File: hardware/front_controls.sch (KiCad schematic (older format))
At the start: 87 parts, among them J1 Conn_01x02, J2 Conn_01x02, J3 Conn_01x02, J4 Conn_01x02, J5 Conn_01x02, J6 Conn_01x02, J7 Conn_01x02, J8 Conn_01x02, J9 Conn_01x02, P2 CONN_01X10, Q1 Q_PNP_BEC, U1 Adafruit_Metro_Mini, U10 G3VM-31BR, U2 G3VM-31BR, U3 G3VM-31BR, U4 G3VM-31BR, U5 G3VM-31BR, U6 G3VM-31BR, U7 G3VM-31BR, U8 G3VM-31BR, U9 G3VM-31BR

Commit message: Version 2 hardware files
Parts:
- removed D20, D21: D_Schottky, Diode_SMD:D_SMC, symbol Device:D_Schottky
- removed Q1: Q_PNP_BEC, Package_TO_SOT_SMD:SOT-23, symbol Device:Q_PNP_BEC
- removed U1: Adafruit_Metro_Mini, Adafruit:DIP-28_W15.24mm, symbol front_controls-rescue:Adafruit_Metro_Mini
- added A1: Arduino_Nano_v3.x, NANO:Arduino_Nano, symbol MCU_Module:Arduino_Nano_v3.x
- added C11, C12: 33pf, Capacitor_SMD:C_0402_1005Metric, symbol Device:C_Small
- added C13, C14, C15, C16: 100nf, Capacitor_SMD:C_0402_1005Metric, symbol Device:C_Small
- added C17: 330uf, Capacitor_THT:CP_Radial_D8.0mm_P3.50mm, symbol Device:CP1_Small
- added Cboot1: 0.1uf, Capacitor_SMD:C_0402_1005Metric, symbol Device:C
- added Chf1: 220nf, Capacitor_SMD:C_0805_2012Metric, symbol Device:C
- added Cin1: 10uf, Capacitor_SMD:C_0805_2012Metric, symbol Device:C
- added Cout1, Cout2, Cout3, Cout4: 22uF, Capacitor_SMD:C_0805_2012Metric, symbol Device:C
- added D20: 15V standoff, Diode_SMD:D_SMB, symbol Device:D_TVS
- added J10: Conn_01x02, Connector_PinHeader_2.54mm:PinHeader_1x02_P2.54mm_Vertical, symbol Connector_Generic:Conn_01x02
- added L1: 8uH, 14m, Inductor_SMD:L_Bourns_SRP7028A_7.3x6.6mm, symbol Device:L_Small
- added P1: PWR, Connector_JST:JST_EH_B2B-EH-A_1x02_P2.50mm_Vertical, symbol Connector_Generic:Conn_01x02
- added P3: HM-10, Connector_PinSocket_2.54mm:PinSocket_1x06_P2.54mm_Vertical, symbol Connector_Generic:Conn_01x06
- added P4: Conn_01x06, Connector_PinHeader_2.54mm:PinHeader_1x06_P2.54mm_Vertical, symbol Connector_Generic:Conn_01x06
- added R10, R14, R15, R18, R19, R9: 1k, Resistor_SMD:R_0402_1005Metric, symbol Device:R
- added R42: 4K7 1%, Resistor_SMD:R_0402_1005Metric, symbol front_controls-rescue:R
- added R43, R44: 100k, Resistor_SMD:R_0402_1005Metric, symbol front_controls-rescue:R
- added Rfbb1: 24K9 1%, Resistor_SMD:R_0402_1005Metric, symbol Device:R
- added Rfbt1: 100k 1%, Resistor_SMD:R_0402_1005Metric, symbol Device:R
- added U12: LMR33630ADDA, NANO:Texas_HSOP-8-1EP_3.9x4.9mm_P1.27mm_ThermalVias, symbol Regulators:LMR33630ADDA
- added U13: MCP23017-E/SO, Package_SO:SOIC-28W_7.5x18.7mm_P1.27mm, symbol Interface_Expansion:MCP23017_SO
- added U14: MCP2515-xSO, Package_SO:SOIC-18W_7.5x11.6mm_P1.27mm, symbol Interface_CAN_LIN:MCP2515-xSO
- added U15: TJA1051T, Package_SO:SOIC-8_3.9x4.9mm_P1.27mm, symbol Interface_CAN_LIN:TJA1051T
- added Y1: 12Mhz, Crystal:Crystal_SMD_3225-4Pin_3.2x2.5mm, symbol Device:Crystal_GND24_Small
- D1, D14, D15, D16, D17, D18, D19, D2, D3, D4, D5, D6: footprint Diode_SMD:D_SMC -> Diode_SMD:D_SOD-123; LCSC C35722 -> C8598
- D10, D11, D12, D13, D8, D9: value 4.7 -> 4.7V Zener; footprint Diode_SMD:D_SMB -> Diode_SMD:D_SOD-323; LCSC C188530 -> C136181
- D7: value 5.1 -> 5.1V Zener
- R0: renamed from R1; value 500 -> 500R
- R1: renamed from R2; value 500 -> 500R
- R2: renamed from R3; value 500 -> 500R
- R24: value 10 -> 10R
- R27: renamed from R25; value 10 -> 10R
- R3: renamed from R30; value 500 -> 500R
- R30: renamed from R26; value 10 -> 10R
- R33: renamed from R27; value 10 -> 10R
- R36: renamed from R28; value 10 -> 10R
- R39: renamed from R29; value 10 -> 10R
- R4: renamed from R31; value 500 -> 500R
- R40: renamed from R10; value 10 -> 10R
- R5: renamed from R32; value 500 -> 500R
- R6: renamed from R33; value 500 -> 500R
- R7: renamed from R34; value 500 -> 500R
- R8: renamed from R35; value 500 -> 500R
- renumbered R4 to R12, R7 to R13, R5 to R16, R8 to R17, R6 to R20, R9 to R21, R12 to R22, R18 to R23, R13 to R25, R19 to R26, R14 to R28, R20 to R29, R15 to R31, R21 to R32, R16 to R34, R22 to R35, R17 to R37, R23 to R38, R11 to R41
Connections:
- net GND: now also A1.29 (GND), A1.4 (GND), C11.1, C12.1, C13.2, C14.1, C15.2, C16.2, C17.2, Chf1.1, Cin1.1, Cout1.2, Cout2.2, Cout3.2, Cout4.2, D20.1 (A1), P1.1 (Pin_1), P3.4 (Pin_4), P4.6 (Pin_6), R10.2, R15.2, R19.2, R42.2, Rfbb1.2, U12.1 (PGND), U12.9 (AGND), U13.10 (VSS), U14.9 (VSS), U15.2 (GND), U15.8 (S), Y1.2, Y1.4; no longer D2.2 (A), D4.2 (A), D6.2 (A)
- net VCC: now also A1.27 (+5V), C13.1, C14.2, C15.1, C16.1, Cout1.1, Cout2.1, Cout3.1, Cout4.1, L1.1, P3.5 (Pin_5), R43.2, R44.1, Rfbt1.2, U13.9 (VDD), U14.18 (VDD), U15.3 (VCC)
- net OUT_U7: now reaches U7.1
- net OUT_U7: now also U13.6 (GPB5)
- net OUT_U8: now reaches U8.1
- net OUT_U8: now also U13.7 (GPB6)
- net OUT_U9: now reaches U9.1
- net OUT_U9: now also U13.8 (GPB7)
- net OUT_U10: now reaches U10.1
- net OUT_U10: now also U13.21 (GPA0)
- net IN_AN1: now reaches C4.1, D7.1 (K), R40.2, R41.1
- net IN_AN1: now also A1.25 (A6)
- net IN_LOW1: now reaches C1.1, R12.2, R13.2
- net IN_LOW1: now also U13.22 (GPA1)
- net IN_LOW2: now reaches C2.1, R16.2, R17.2
- net IN_LOW2: now also U13.23 (GPA2)
- net IN_LOW3: now reaches C3.1, R20.2, R21.2
- net IN_LOW3: now also U13.24 (GPA3)
- net OUT_U3: now reaches U3.1
- net OUT_U3: now also U13.2 (GPB1)
- net OUT_U4: now reaches U4.1
- net OUT_U4: now also U13.3 (GPB2)
- net IN_HIGH6: now reaches C10.1, D13.1 (K), R37.1, R38.1
- net IN_HIGH6: now also A1.5 (D2)
- net IN_HIGH5: now reaches C9.1, D12.1 (K), R34.1, R35.1
- net IN_HIGH5: now also A1.7 (D4)
- net IN_HIGH4: now reaches C8.1, D11.1 (K), R31.1, R32.1
- net IN_HIGH4: now also A1.8 (D5)
- net IN_HIGH3: now reaches C7.1, D10.1 (K), R28.1, R29.1
- net IN_HIGH3: now also U13.27 (GPA6)
- net IN_HIGH2: now reaches C6.1, D9.1 (K), R25.1, R26.1
- net IN_HIGH2: now also U13.26 (GPA5)
- net IN_HIGH1: now reaches C5.1, D8.1 (K), R22.1, R23.1
- net IN_HIGH1: now also U13.25 (GPA4)
- net OUT_U5: now reaches U5.1
- net OUT_U5: now also U13.4 (GPB3)
- net OUT_U6: now reaches U6.1
- net OUT_U6: now also U13.5 (GPB4)
- net at P2.10 (P10): now also R9.2; no longer D1.1 (K)
- net at P2.8 (P8): now also R18.2; no longer D5.1 (K)
- net at P2.9 (P9): now also R14.2; no longer D3.1 (K)
- net OUT_U2: now reaches U2.1
- net OUT_U2: now also U13.1 (GPB0)
- new net: D1.1 (K), R9.1
- new net: D2.2 (A), R10.1
- new net: D3.1 (K), R14.1
- new net: D4.2 (A), R15.1
- new net: D5.1 (K), R18.1
- new net: D6.2 (A), R19.1
- new net: C17.1, Chf1.2, Cin1.2, D20.2 (A2), P1.2 (Pin_2), U12.2 (VIN), U12.3 (EN)
- new net: Rfbb1.1, Rfbt1.1, U12.5 (FB)
- new net: Cboot1.1, L1.2, U12.7 (BOOT)
- new net: Cboot1.2, U12.8 (SW)
- new net: R42.1, U13.15 (A0), U13.16 (A1), U13.17 (A2)
- new net: R44.2, U13.18 (~RESET~)
- new net: R43.1, U14.17 (~RESET)
- new net: C12.2, U14.7 (OSC2), Y1.3
- new net: C11.2, U14.8 (OSC1), Y1.1
- new net BT_EN: A1.12 (D9), P3.6 (Pin_6)
- new net BT_RX: A1.10 (D7), P3.2 (Pin_2)
- new net BT_STATE: P3.1 (Pin_1), U13.28 (GPA7)
- new net BT_TX: A1.11 (D8), P3.3 (Pin_3)
- new net CAN_H: J10.1 (Pin_1), U15.7 (CANH)
- new net CAN_INT: A1.20 (A1), U14.12 (~INT)
- new net CAN_L: J10.2 (Pin_2), U15.6 (CANL)
- new net INTA1: A1.6 (D3), U13.20 (INTA)
- new net OUT_11: A1.9 (D6), P4.1 (Pin_1)
- new net OUT_12: A1.26 (A7), P4.2 (Pin_2)
- new net OUT_13: A1.22 (A3), P4.3 (Pin_3)
- new net OUT_14: A1.21 (A2), P4.4 (Pin_4)
- new net OUT_15: A1.19 (A0), P4.5 (Pin_5)
- new net RXCAN: U14.2 (RXCAN), U15.4 (RXD)
- new net SCL: A1.24 (A5), U13.12 (SCK)
- new net SDA: A1.23 (A4), U13.13 (SDA)
- new net SPI_CS: A1.13 (D10), U14.16 (~CS)
- new net SPI_SCK: A1.16 (D13), U14.13 (SCK)
- new net SPI_SI: A1.14 (D11), U14.14 (SI)
- new net SPI_SO: A1.15 (D12), U14.15 (SO)
- new net TXCAN: U14.1 (TXCAN), U15.1 (TXD)
- no-connect marks 8 -> 0
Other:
- moved on the sheet: C4, D7, R40, R41

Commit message: Hardware V2 major modifications
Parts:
- removed C17: 330uf, Capacitor_THT:CP_Radial_D8.0mm_P3.50mm, symbol Device:CP1_Small
- removed Cboot1: 0.1uf, Capacitor_SMD:C_0402_1005Metric, symbol Device:C
- removed Chf1: 220nf, Capacitor_SMD:C_0805_2012Metric, symbol Device:C
- removed Cin1: 10uf, Capacitor_SMD:C_0805_2012Metric, symbol Device:C
- removed Cout1, Cout2, Cout3, Cout4: 22uF, Capacitor_SMD:C_0805_2012Metric, symbol Device:C
- removed D20: 15V standoff, Diode_SMD:D_SMB, symbol Device:D_TVS
- removed L1: 8uH, 14m, Inductor_SMD:L_Bourns_SRP7028A_7.3x6.6mm, symbol Device:L_Small
- removed Rfbb1: 24K9 1%, Resistor_SMD:R_0402_1005Metric, symbol Device:R
- removed Rfbt1: 100k 1%, Resistor_SMD:R_0402_1005Metric, symbol Device:R
- removed U12: LMR33630ADDA, NANO:Texas_HSOP-8-1EP_3.9x4.9mm_P1.27mm_ThermalVias, symbol Regulators:LMR33630ADDA
- added H? (x4): MountingHole, MountingHole:MountingHole_2.7mm_M2.5, symbol Mechanical:MountingHole
- added J11: CAN, Connector_JST:JST_EH_B2B-EH-A_1x02_P2.50mm_Vertical, symbol Connector_Generic:Conn_01x02
- added JP1: Jumper_NO_Small, Jumper:SolderJumper-2_P1.3mm_Open_RoundedPad1.0x1.5mm, symbol Device:Jumper_NO_Small
- added P2: PWR, Connector_JST:JST_EH_B2B-EH-A_1x02_P2.50mm_Vertical, symbol Connector_Generic:Conn_01x02
- added R11, R45: 4k7, Resistor_SMD:R_0603_1608Metric, symbol Device:R_Small
- added R46: 120R, Resistor_SMD:R_0402_1005Metric, symbol Device:R_Small
- added U1: TXB0104PW, Package_SO:TSSOP-14_4.4x5mm_P0.65mm, symbol Logic_LevelTranslator:TXB0104PW
- C4: value .01uf -> .1uf; LCSC C15195 -> C1525
- H3: renamed from P4; value Conn_01x06 -> Expansion; footprint Connector_PinHeader_2.54mm:PinHeader_1x06_P2.54mm_Vertical -> Connector_PinHeader_2.54mm:PinHeader_2x08_P2.54mm_Vertical; symbol Connector_Generic:Conn_01x06 -> Connector_Generic:Conn_02x08_Odd_Even
- J10: value Conn_01x02 -> CAN; footprint Connector_PinHeader_2.54mm:PinHeader_1x02_P2.54mm_Vertical -> Connector_JST:JST_EH_B2B-EH-A_1x02_P2.50mm_Vertical
- R40: value 10R -> 10k; footprint Resistor_SMD:R_0402_1005Metric -> Resistor_SMD:R_0603_1608Metric; LCSC C25077 -> C25804
- R41: value 1k -> 2k2; footprint Resistor_SMD:R_0402_1005Metric -> Resistor_SMD:R_0603_1608Metric; LCSC C11702 -> C4190
- renumbered P2 to H1, P3 to H2
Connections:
- net CAN_H: now also J11.1 (Pin_1), JP1.1
- net CAN_L: now also J11.2 (Pin_2), R46.1
- net GND: now also H3.1 (Pin_1), H3.14 (Pin_14), P2.1 (Pin_1), U1.7 (GND); no longer H3.6 (Pin_6), P1.1 (Pin_1)
- net SCL: now also H3.7 (Pin_7), R11.1
- net SDA: now also H3.9 (Pin_9), R45.2
- net SPI_SCK: now also H3.12 (Pin_12)
- net SPI_SI: now also H3.8 (Pin_8)
- net SPI_SO: now also H3.10 (Pin_10)
- net VCC: now also H3.2 (Pin_2), R11.2, R45.1, U1.14 (VCCB), U1.8 (OE)
- net VIN: now reaches P1.2 (Pin_2)
- net VIN: now also H3.16 (Pin_16), P2.2 (Pin_2)
- net UART_TX: now reaches A1.1 (D1/TX)
- net UART_TX: now also H3.6 (Pin_6)
- net 3V3: now reaches A1.17 (3V3)
- net 3V3: now also U1.1 (VCCA)
- net UART_RX: now reaches A1.2 (D0/RX)
- net UART_RX: now also H3.4 (Pin_4)
- net BT_RX renamed BT_RX_H
- net BT_RX_H: now also U1.12 (B2); no longer H2.2 (Pin_2)
- net BT_TX renamed BT_TX_H
- net BT_TX_H: now also U1.13 (B1); no longer H2.3 (Pin_3)
- net IN_HIGH1 renamed IN_HORN
- net IN_HIGH2 renamed IN_HL_HIGH
- net IN_HIGH3 renamed IN_KILL
- net IN_HIGH4 renamed IN_RIGHT
- net IN_HIGH5 renamed IN_LEFT
- net IN_HIGH6 renamed IN_BRAKE
- net IN_LOW1 renamed IN_CLUTCH
- net IN_LOW2 renamed IN_KICK
- net IN_LOW3 renamed IN_NEUTRAL
- net OUT_11 renamed MCU_D6
- net MCU_D6: now also H3.3 (Pin_3); no longer H3.1 (Pin_1)
- net OUT_12 renamed MCU_A7
- net MCU_A7: now also H3.5 (Pin_5); no longer H3.2 (Pin_2)
- net OUT_13 renamed MCU_A3
- net MCU_A3: now also H3.11 (Pin_11); no longer H3.3 (Pin_3)
- net OUT_14 renamed MCU_A2
- net MCU_A2: now also H3.13 (Pin_13); no longer H3.4 (Pin_4)
- net OUT_15 renamed MCU_A0
- net MCU_A0: now also H3.15 (Pin_15); no longer H3.5 (Pin_5)
- net OUT_U10 renamed OUT_HORN
- net OUT_U2 renamed OUT_LEFT
- net OUT_U3 renamed OUT_RIGHT
- net OUT_U4 renamed OUT_REAR
- net OUT_U5 renamed OUT_BRAKE
- net OUT_U6 renamed OUT_START_EN
- net OUT_U7 renamed OUT_HL_HIGH
- net OUT_U8 renamed OUT_HL_LOW
- net OUT_U9 renamed OUT_RUNNING
- new net: JP1.2, R46.2
- new net BT_RX_L: H2.2 (Pin_2), U1.3 (A2)
- new net BT_TX_L: H2.3 (Pin_3), U1.2 (A1)
- new net Switching Regulator (5V)/GND: P1.1 (Pin_1)
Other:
- moved on the sheet: A1, C11, C12, C13, C14, C15, C16, H2, R42, R43, R44, U13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

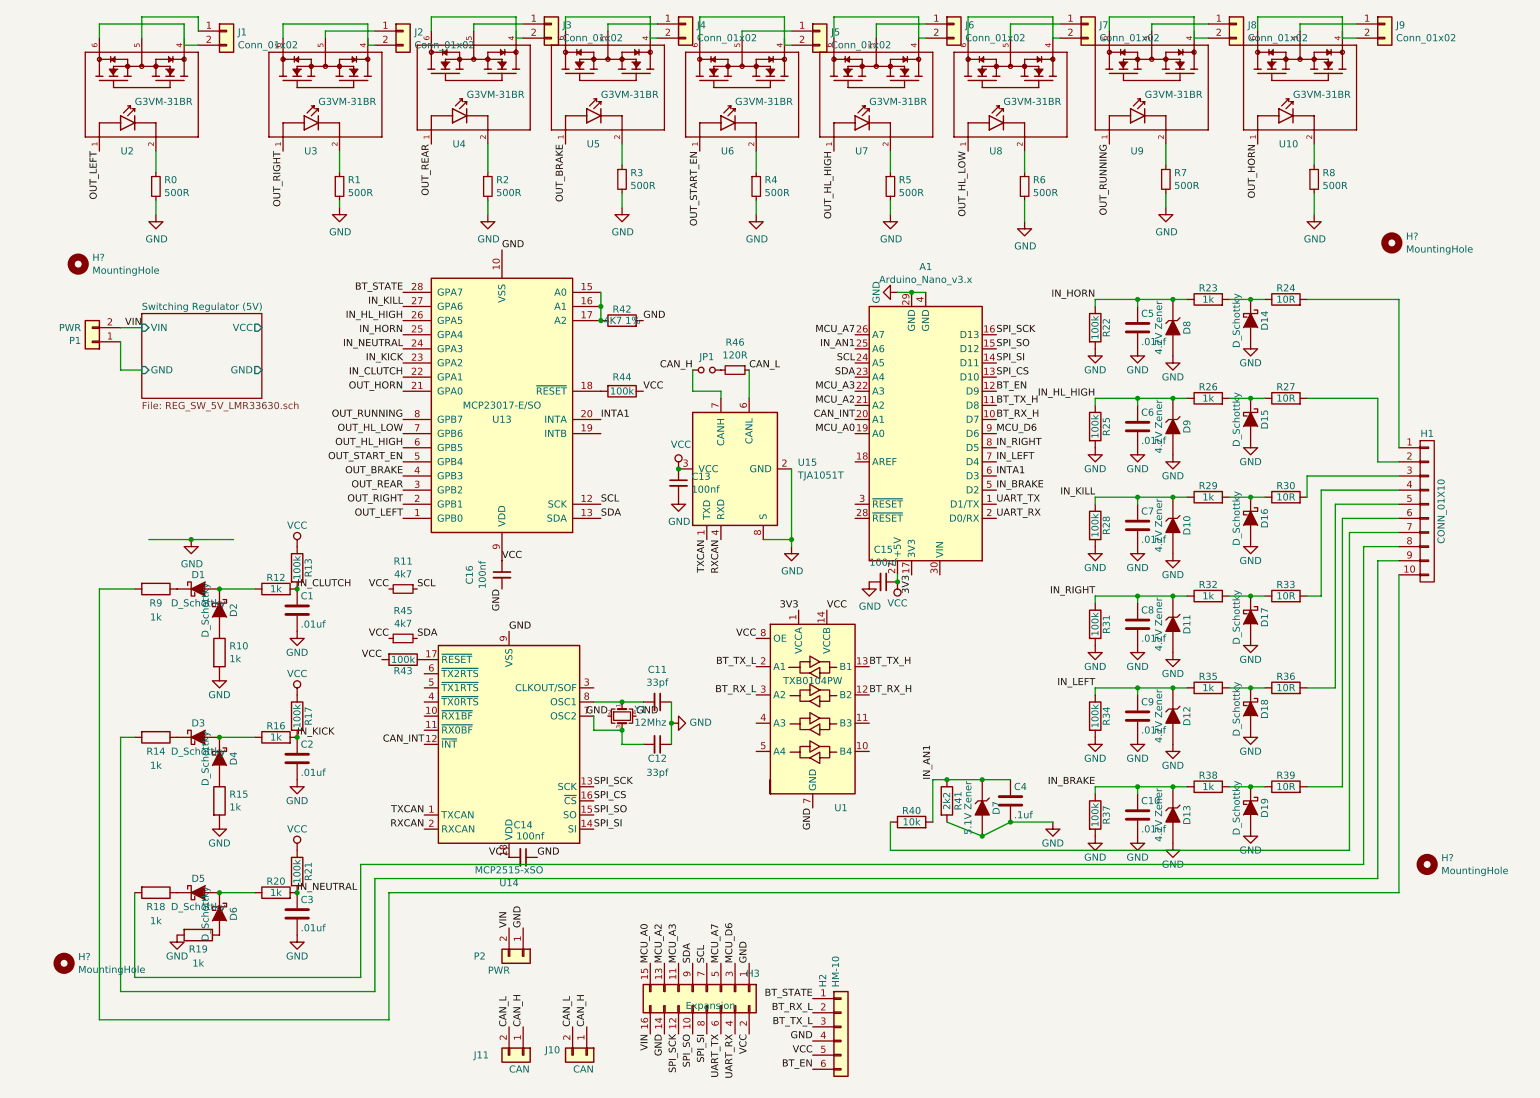
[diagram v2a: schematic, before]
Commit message: Switched regulators to more available chip
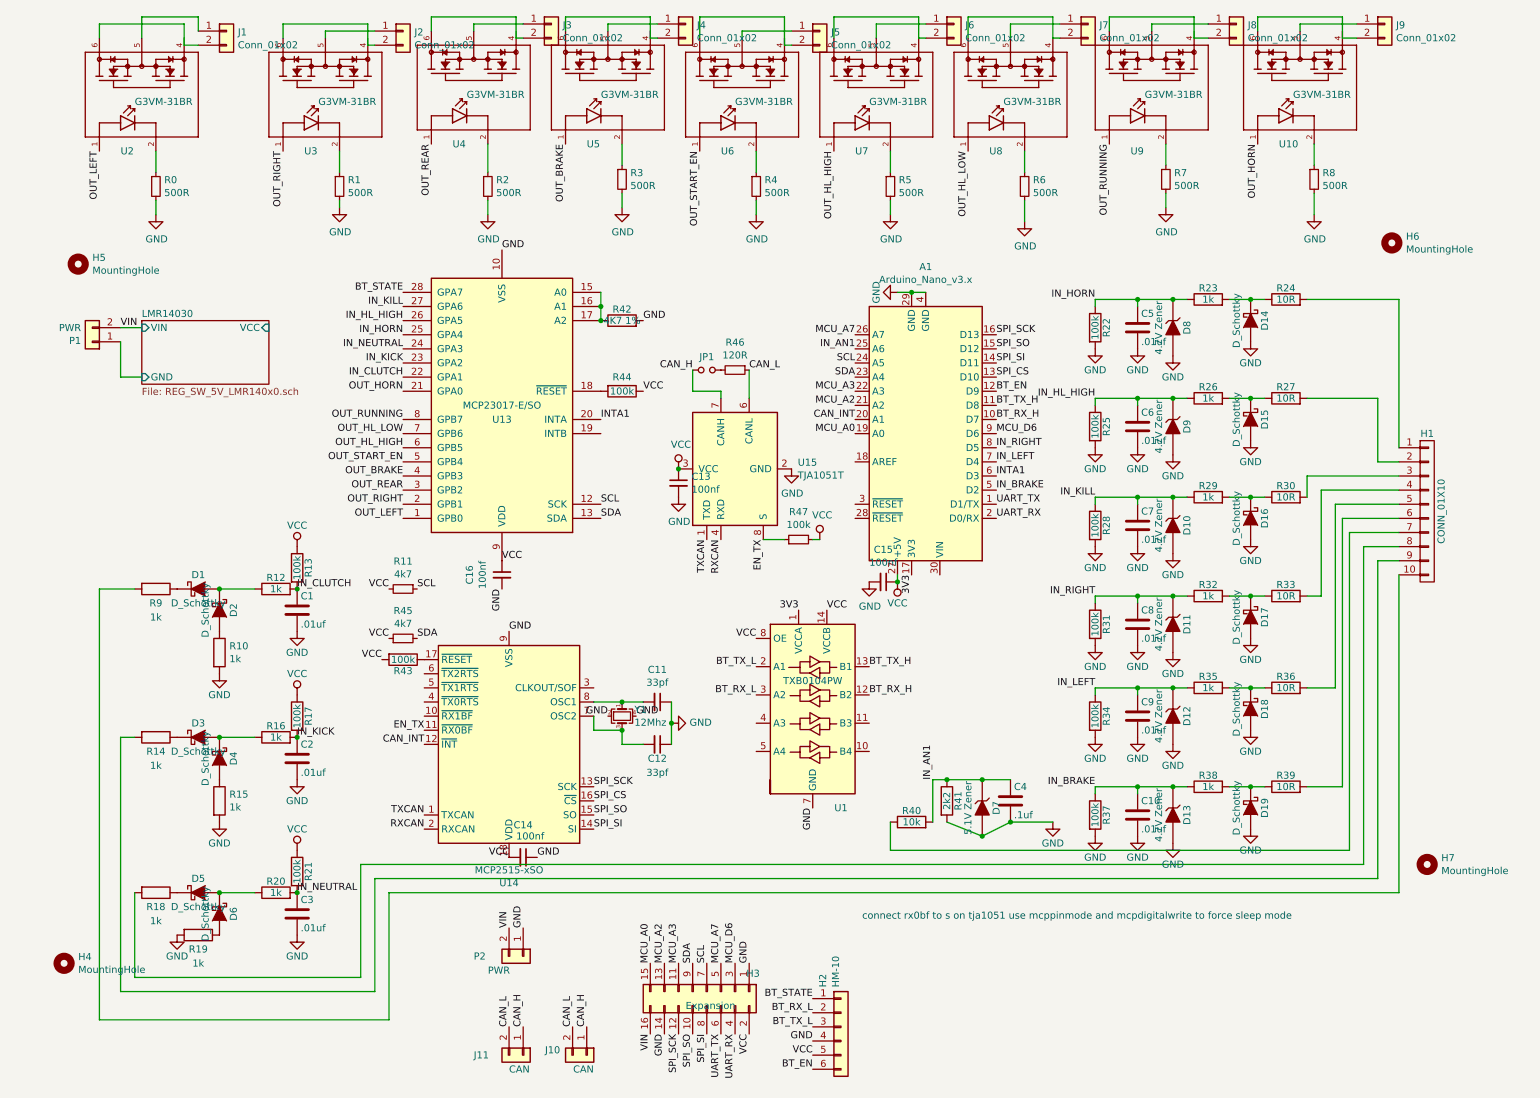
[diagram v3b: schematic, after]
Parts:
- added R47: 100k, Resistor_SMD:R_0402_1005Metric, symbol Device:R_Small
- gave numbers to parts that had none: 4
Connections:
- net GND: no longer U15.8 (S)
- net VCC: now also R47.2
- net EN_TX: now reaches U14.11 (~RX0BF)
- net EN_TX: now also U15.8 (S), R47.1
- net Switching Regulator (5V)/GND renamed LMR14030/GND
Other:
- note added: "connect rx0bf to s on tja1051 use mcppinmode and mcpdigitalwrite to force sleep mode"
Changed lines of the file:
@@
 $EndComp
-$Comp
-L power:GND #PWR0113
-U 1 1 6073990D
-P 1600 4200
-F 0 "#PWR0113" H 1600 3950 50  0001 C CNN
-F 1 "GND" H 1605 4027 50  0000 C CNN
-F 2 "" H 1600 4200 50  0001 C CNN
-F 3 "" H 1600 4200 50  0001 C CNN
-	1    1600 4200
-	1    0    0    -1
-$EndComp
-Connection ~ 1600 4200
 $Comp
 L Device:R R19
@@
 L power:GND #PWR0116
 U 1 1 60E22969
-P 5850 4250
-F 0 "#PWR0116" H 5850 4000 50  0001 C CNN
-F 1 "GND" H 5855 4077 50  0000 C CNN
-F 2 "" H 5850 4250 50  0001 C CNN
-F 3 "" H 5850 4250 50  0001 C CNN
-	1    5850 4250
-	1    0    0    -1
-$EndComp
-Wire Wire Line
-	5850 3700 5850 4200
-Wire Wire Line
-	5650 4200 5850 4200
-Connection ~ 5850 4200
-Wire Wire Line
-	5850 4200 5850 4250
+P 5850 3700
+F 0 "#PWR0116" H 5850 3450 50  0001 C CNN
+F 1 "GND" H 5855 3527 50  0000 C CNN
+F 2 "" H 5850 3700 50  0001 C CNN
+F 3 "" H 5850 3700 50  0001 C CNN
+	1    5850 3700
+	1    0    0    -1
+$EndComp
 $Comp
 L power:GND #PWR0117
@@
 Text Label 6000 6100 3    50   ~ 0
 GND
-Wire Wire Line
-	1300 4200 1600 4200
-Wire Wire Line
-	1600 4200 1900 4200
-$Sheet
-S 1250 2600 850  600
-U 60F4CB3B
-F0 "Switching Regulator (5V)" 50
-F1 "REG_SW_5V_LMR33630.sch" 50
-F2 "VCC" O R 2100 2700 50
-F3 "GND" O R 2100 3000 50
-F4 "VIN" I L 1250 2700 50
-F5 "GND" I L 1250 3000 50
-$EndSheet
 $Comp
 L Device:R_Small R46
@@
 	-1   0    0    1
 $EndComp
-Wire Wire Line
-	1100 2700 1250 2700
-Wire Wire Line
-	1100 2800 1100 3000
-Wire Wire Line
-	1100 3000 1250 3000
 Text Label 3950 6950 1    50   ~ 0
 GND
@@
 Text Label 5450 7700 3    50   ~ 0
 UART_RX
-Text Label 1250 2700 2    50   ~ 0
-VIN
-$Comp
-L Mechanical:MountingHole H?
+$Comp
+L Mechanical:MountingHole H6
 U 1 1 60A2666F
 P 10100 2100
-F 0 "H?" H 10200 2146 50  0000 L CNN
+F 0 "H6" H 10200 2146 50  0000 L CNN
 F 1 "MountingHole" H 10200 2055 50  0000 L CNN
 F 2 "MountingHole:MountingHole_2.7mm_M2.5" H 10100 2100 50  0001 C CNN
@@
 $EndComp
 $Comp
-L Mechanical:MountingHole H?
+L Mechanical:MountingHole H5
 U 1 1 60A2D26A
 P 800 2250
-F 0 "H?" H 900 2296 50  0000 L CNN
+F 0 "H5" H 900 2296 50  0000 L CNN
 F 1 "MountingHole" H 900 2205 50  0000 L CNN
 F 2 "MountingHole:MountingHole_2.7mm_M2.5" H 800 2250 50  0001 C CNN
@@
 $EndComp
 $Comp
-L Mechanical:MountingHole H?
+L Mechanical:MountingHole H4
 U 1 1 60A2F287
 P 700 7200
-F 0 "H?" H 800 7246 50  0000 L CNN
+F 0 "H4" H 800 7246 50  0000 L CNN
 F 1 "MountingHole" H 800 7155 50  0000 L CNN
 F 2 "MountingHole:MountingHole_2.7mm_M2.5" H 700 7200 50  0001 C CNN
@@
 $EndComp
 $Comp
-L Mechanical:MountingHole H?
+L Mechanical:MountingHole H7
 U 1 1 60A37691
 P 10350 6500
-F 0 "H?" H 10450 6546 50  0000 L CNN
+F 0 "H7" H 10450 6546 50  0000 L CNN
 F 1 "MountingHole" H 10450 6455 50  0000 L CNN
 F 2 "MountingHole:MountingHole_2.7mm_M2.5" H 10350 6500 50  0001 C CNN
@@
 	1    0    0    -1
 $EndComp
+Text Notes 6350 6900 0    50   ~ 0
+connect rx0bf to s on tja1051 use mcppinmode and mcpdigitalwrite to force sleep mode
+Text Label 5650 4200 3    50   ~ 0
+EN_TX
+Text Label 3250 5550 2    50   ~ 0
+EN_TX
+$Comp
+L Device:R_Small R47
+U 1 1 60AD961C
+P 5900 4200
+F 0 "R47" V 6096 4200 50  0000 C CNN
+F 1 "100k" V 6005 4200 50  0000 C CNN
+F 2 "Resistor_SMD:R_0402_1005Metric" H 5900 4200 50  0001 C CNN
+F 3 "" H 5900 4200 50  0001 C CNN
+F 4 "C25741" H 5900 4200 50  0001 C CNN "LCSC"
+	1    5900 4200
+	0    -1   -1   0
+$EndComp
+$Comp
+L power:VCC #PWR0110
+U 1 1 60ADDA65
+P 6050 4200
+F 0 "#PWR0110" H 6050 4050 50  0001 C CNN
+F 1 "VCC" H 6067 4373 50  0000 C CNN
+F 2 "" H 6050 4200 50  0001 C CNN
+F 3 "" H 6050 4200 50  0001 C CNN
+	1    6050 4200
+	1    0    0    -1
+$EndComp
+Wire Wire Line
+	5800 4200 5650 4200
+Wire Wire Line
+	6000 4200 6050 4200
+$Sheet
+S 1250 2650 900  450
+U 60B4A6B3
+F0 "LMR14030" 50
+F1 "REG_SW_5V_LMR140x0.sch" 50
+F2 "VCC" I R 2150 2700 50
+F3 "VIN" I L 1250 2700 50
+F4 "GND" I L 1250 3050 50
+$EndSheet
+Wire Wire Line
+	1100 2700 1250 2700
+Wire Wire Line
+	1100 2800 1100 3050
+Wire Wire Line
+	1100 3050 1250 3050
+Text Label 1100 2700 0    50   ~ 0
+VIN
 $EndSCHEMATC
